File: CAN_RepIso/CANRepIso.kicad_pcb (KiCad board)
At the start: 4 copper layers, 60 x 27 mm, 53 parts, among them J1 RBUS_IN, J2 RBUS_OUT, U1 SN74LV32ADGVR, U2 SN74LVC2G08DCUR, U3 SN74LVC2G07DBVR, U4 SN74LVC2G07DBVR, U5 SN74LVC2G132DCUR, U6 SN65HVD230, U7 PLACEHOLDER ISOLATOR, U8 SN65HVD230

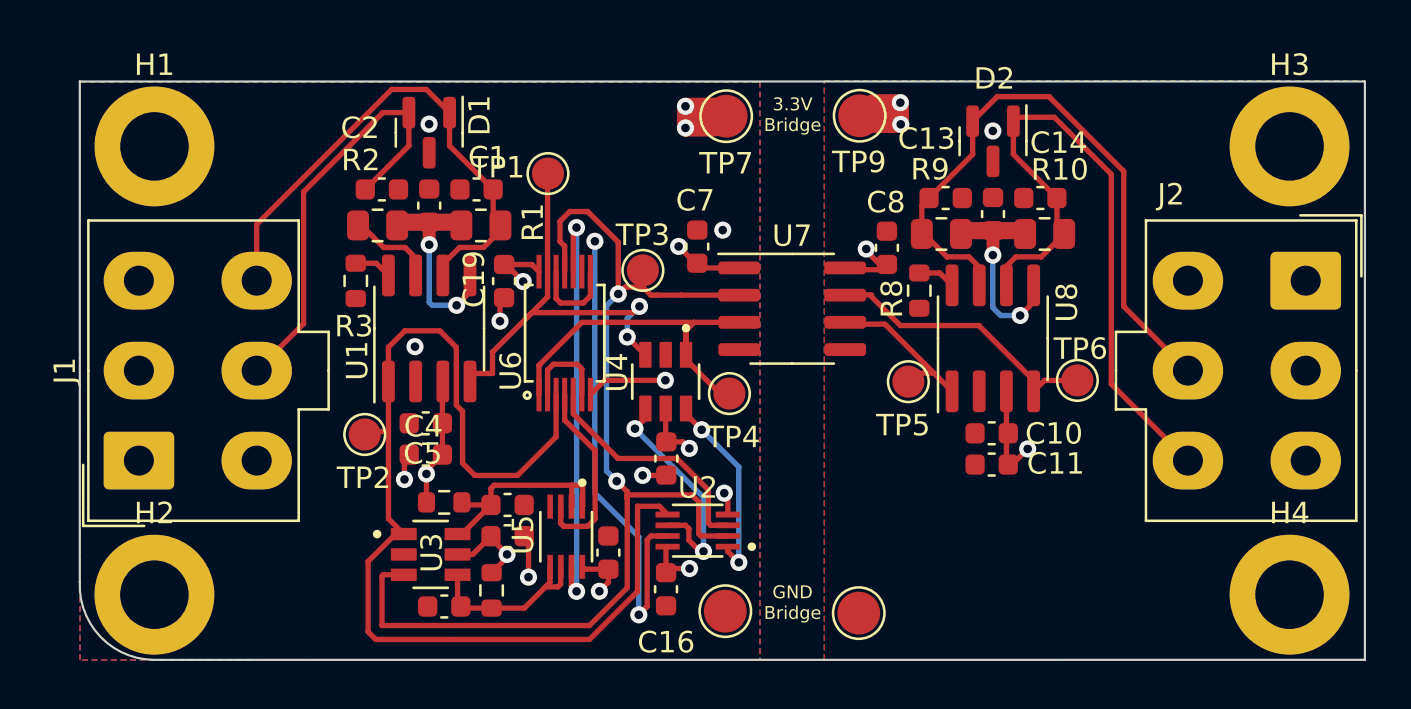
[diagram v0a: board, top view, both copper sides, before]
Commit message: Rounded corners + via stitching
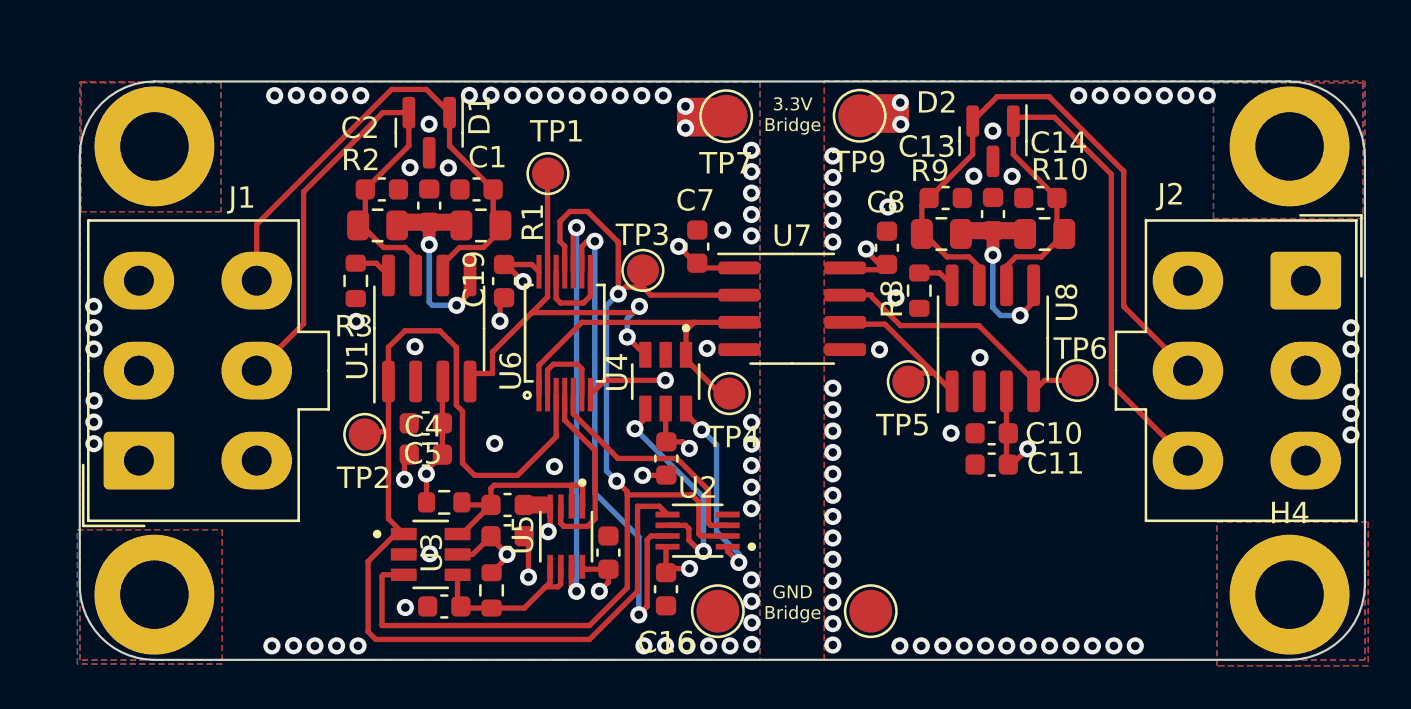
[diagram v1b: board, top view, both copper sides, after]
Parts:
- moved TP10 0.57 mm to (69.7, 106.5)
- moved TP8 0.35 mm to (62.5, 106.5)
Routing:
- net +3V3: track 31.8 -> 28.7 mm
- net /CAN_LOW_IN: track 26.2 -> 23.8 mm
- net +3.3VA: track 15.2 -> 12.8 mm
- net Net-(U1-Pad9): track 23.0 -> 24.9 mm
- net /Vref: track 9.87 -> 8.61 mm
- net /Vref2: track 9.73 -> 8.51 mm
- net /CAN_HIGH_OUT: track 29.9 -> 29.0 mm
- net /TX2: track 16.9 -> 16.1 mm
- net /CAN_LOW_OUT: track 31.3 -> 30.6 mm
- net /TX1: track 51.5 -> 50.9 mm
- net Net-(TP5-Pad1): track 7.65 -> 7.08 mm
- net Net-(TP6-Pad1): track 13.2 -> 12.7 mm
- net GND: track 10.4 -> 10.7 mm, vias 9 -> 62
- net GND1: vias 1 -> 50
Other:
- outline, holes or cut-outs redrawn

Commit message: changed U4 from driver to NOT gate, implemented review feedback
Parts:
- U4: value SN74LVC2G07DBVR -> SN74LVC2G04DBVR
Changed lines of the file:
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@@
     (property "Sheetname" "Bus Arbitration")
     (attr smd)
-    (fp_text reference "R12" (at 0.3 -1.3925 90) (layer "F.SilkS") hide
+    (fp_text reference "R12" (at 0.12 -1.3825 90) (layer "F.SilkS")
       (effects (font (size 1 1) (thickness 0.15)))
     )
@@
     (property "Sheetname" "Bus Arbitration")
     (attr through_hole)
-    (fp_text reference "U4" (at -0.43 2.26 -90) (layer "F.SilkS")
-      (effects (font (size 1 1) (thickness 0.15)))
-    )
-    (fp_text value "SN74LVC2G07DBVR" (at 7.26 2.365 90) (layer "F.Fab")
+    (fp_text reference "U4" (at 0.375 -2.635 -90) (layer "F.SilkS")
+      (effects (font (size 1 1) (thickness 0.15)))
+    )
+    (fp_text value "SN74LVC2G04DBVR" (at 7.26 2.365 -90) (layer "F.Fab")
       (effects (font (size 1 1) (thickness 0.15)))
     )
@@
     (fp_line (start -0.8 1.56) (end 0.8 1.56) (layer "F.SilkS") (width 0.127))
     (fp_circle (center -2.5 -0.95) (end -2.4 -0.95) (layer "F.SilkS") (width 0.2) (fill none))
-    (fp_line (start 2.11 1.49) (end 1.05 1.49) (layer "F.CrtYd") (width 0.05))
-    (fp_line (start 1.05 -1.49) (end 1.05 -1.7) (layer "F.CrtYd") (width 0.05))
-    (fp_line (start -1.05 1.7) (end 1.05 1.7) (layer "F.CrtYd") (width 0.05))
     (fp_line (start 1.05 1.49) (end 1.05 1.7) (layer "F.CrtYd") (width 0.05))
     (fp_line (start -2.11 -1.49) (end -2.11 1.49) (layer "F.CrtYd") (width 0.05))
+    (fp_line (start -1.05 -1.49) (end -1.05 -1.7) (layer "F.CrtYd") (width 0.05))
+    (fp_line (start 2.11 -1.49) (end 1.05 -1.49) (layer "F.CrtYd") (width 0.05))
     (fp_line (start 1.05 -1.7) (end -1.05 -1.7) (layer "F.CrtYd") (width 0.05))
+    (fp_line (start -1.05 1.49) (end -1.05 1.7) (layer "F.CrtYd") (width 0.05))
     (fp_line (start -2.11 -1.49) (end -1.05 -1.49) (layer "F.CrtYd") (width 0.05))
-    (fp_line (start -1.05 1.49) (end -1.05 1.7) (layer "F.CrtYd") (width 0.05))
     (fp_line (start -2.11 1.49) (end -1.05 1.49) (layer "F.CrtYd") (width 0.05))
-    (fp_line (start 2.11 -1.49) (end 1.05 -1.49) (layer "F.CrtYd") (width 0.05))
-    (fp_line (start -1.05 -1.49) (end -1.05 -1.7) (layer "F.CrtYd") (width 0.05))
+    (fp_line (start -1.05 1.7) (end 1.05 1.7) (layer "F.CrtYd") (width 0.05))
+    (fp_line (start 1.05 -1.49) (end 1.05 -1.7) (layer "F.CrtYd") (width 0.05))
+    (fp_line (start 2.11 1.49) (end 1.05 1.49) (layer "F.CrtYd") (width 0.05))
     (fp_line (start 2.11 1.49) (end 2.11 -1.49) (layer "F.CrtYd") (width 0.05))
     (fp_line (start 0.8 -1.45) (end -0.8 -1.45) (layer "F.Fab") (width 0.127))
+    (fp_line (start -0.8 -1.45) (end -0.8 1.45) (layer "F.Fab") (width 0.127))
     (fp_line (start -0.8 1.45) (end 0.8 1.45) (layer "F.Fab") (width 0.127))
-    (fp_line (start -0.8 -1.45) (end -0.8 1.45) (layer "F.Fab") (width 0.127))
     (fp_line (start 0.8 1.45) (end 0.8 -1.45) (layer "F.Fab") (width 0.127))
     (fp_circle (center -2.5 -0.95) (end -2.4 -0.95) (layer "F.Fab") (width 0.2) (fill none))
@@
     (property "Sheetname" "Bus Arbitration")
     (attr smd)
-    (fp_text reference "R11" (at 0.08 0.01) (layer "F.SilkS") hide
+    (fp_text reference "R11" (at -2.8425 0.07) (layer "F.SilkS")
       (effects (font (size 1 1) (thickness 0.15)))
     )
@@
     (property "Sheetname" "Bus Arbitration")
     (attr smd)
-    (fp_text reference "C21" (at -0.1025 -0.01) (layer "F.SilkS") hide
+    (fp_text reference "C21" (at 0.0075 -1.36) (layer "F.SilkS")
       (effects (font (size 1 1) (thickness 0.15)))
     )
@@
     (property "Sheetname" "Bus Arbitration")
     (attr smd)
-    (fp_text reference "C18" (at 3 0.01) (layer "F.SilkS") hide
+    (fp_text reference "C18" (at 0.8375 -1.420292) (layer "F.SilkS")
       (effects (font (size 1 1) (thickness 0.15)))
     )
@@
     (property "Sheetname" "")
     (attr exclude_from_pos_files)
-    (fp_text reference "H4" (at 0 -3.8) (layer "F.SilkS")
+    (fp_text reference "H4" (at 0 -3.8) (layer "F.SilkS") hide
       (effects (font (size 1 1) (thickness 0.15)))
     )
@@
     (property "Sheetname" "")
     (attr smd)
-    (fp_text reference "C5" (at 0.14 0.04) (layer "F.SilkS")
+    (fp_text reference "C5" (at -2.435 -0.36) (layer "F.SilkS")
       (effects (font (size 1 1) (thickness 0.15)))
     )
@@
     (property "Sheetname" "Bus Arbitration")
     (attr through_hole)
-    (fp_text reference "U3" (at 0.0575 -0.08 270) (layer "F.SilkS")
+    (fp_text reference "U3" (at -2.8125 0.63 270) (layer "F.SilkS")
       (effects (font (size 1 1) (thickness 0.15)))
     )
@@
     (property "Sheetname" "")
     (attr smd)
-    (fp_text reference "C4" (at 0.11 -0.15) (layer "F.SilkS")
+    (fp_text reference "C4" (at -2.435 0.03) (layer "F.SilkS")
       (effects (font (size 1 1) (thickness 0.15)))
     )
@@
     (property "Sheetname" "Bus Arbitration")
     (attr through_hole)
-    (fp_text reference "U1" (at -1.28 -9.68 90) (layer "F.SilkS")
+    (fp_text reference "U1" (at -1.88 -2.61 90) (layer "F.SilkS")
       (effects (font (size 1.001543 1.001543) (thickness 0.15)))
     )
@@
     (property "Sheetname" "Bus Arbitration")
     (attr smd)
-    (fp_text reference "C19" (at -0.09 1.4 90) (layer "F.SilkS")
+    (fp_text reference "C19" (at 2.1 -0.69 180) (layer "F.SilkS")
       (effects (font (size 1 1) (thickness 0.15)))
     )
@@
     (property "Sheetname" "")
     (attr smd)
-    (fp_text reference "U6" (at -1.99 3.815 90) (layer "F.SilkS")
+    (fp_text reference "U6" (at -2.04 -3.285 90) (layer "F.SilkS")
       (effects (font (size 1 1) (thickness 0.15)))
     )
@@
     (property "Sheetname" "Bus Arbitration")
     (attr through_hole)
-    (fp_text reference "U5" (at -0.09 2.01 90) (layer "F.SilkS")
+    (fp_text reference "U5" (at 3.405 0.2 180) (layer "F.SilkS")
       (effects (font (size 1 1) (thickness 0.15)))
     )
@@
     )
   )
-  (gr_arc (start 32.739117 85.205342) (mid 33.76 82.74) (end 36.225003 81.718297) (layer "Edge.Cuts") (width 0.1))
+  (gr_arc (start 32.739117 85.205342) (mid 33.76 82.739999) (end 36.225003 81.718297) (layer "Edge.Cuts") (width 0.1))
   (gr_line (start 32.739117 85.205342) (end 32.739521 105.084438) (layer "Edge.Cuts") (width 0.1))
   (gr_arc (start 89.219839 81.72) (mid 91.70913 82.752606) (end 92.74 85.242616) (layer "Edge.Cuts") (width 0.1))

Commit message: Added text and logos
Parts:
- added G***: LOGO, iclr:iclr_logo, F.Cu at (78.3, 104.1)
- added G***: LOGO, iclr:spider-man, B.Cu at (65.1, 95.9)
- renumbered J1 to RBUS1, J2 to RBUS2
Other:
- board text added: "CAN BUS REPEATER"
- board text added: "Designed By Andrei Paduraru Electronics and Payload 2022"
- board text added: "Isolator?"
- board text added: "JLCJLCJLCJLC"
- board text added: "No"
- board text added: "Yes"

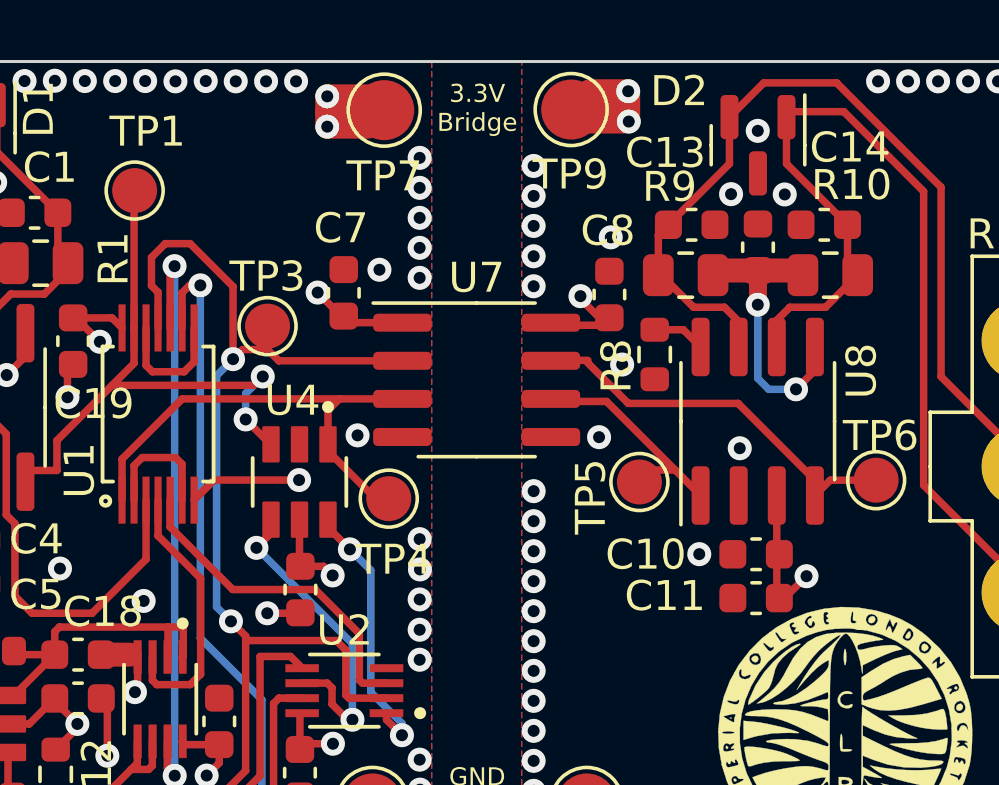
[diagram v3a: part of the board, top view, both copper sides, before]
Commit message: added option for a 2nd digital isolator
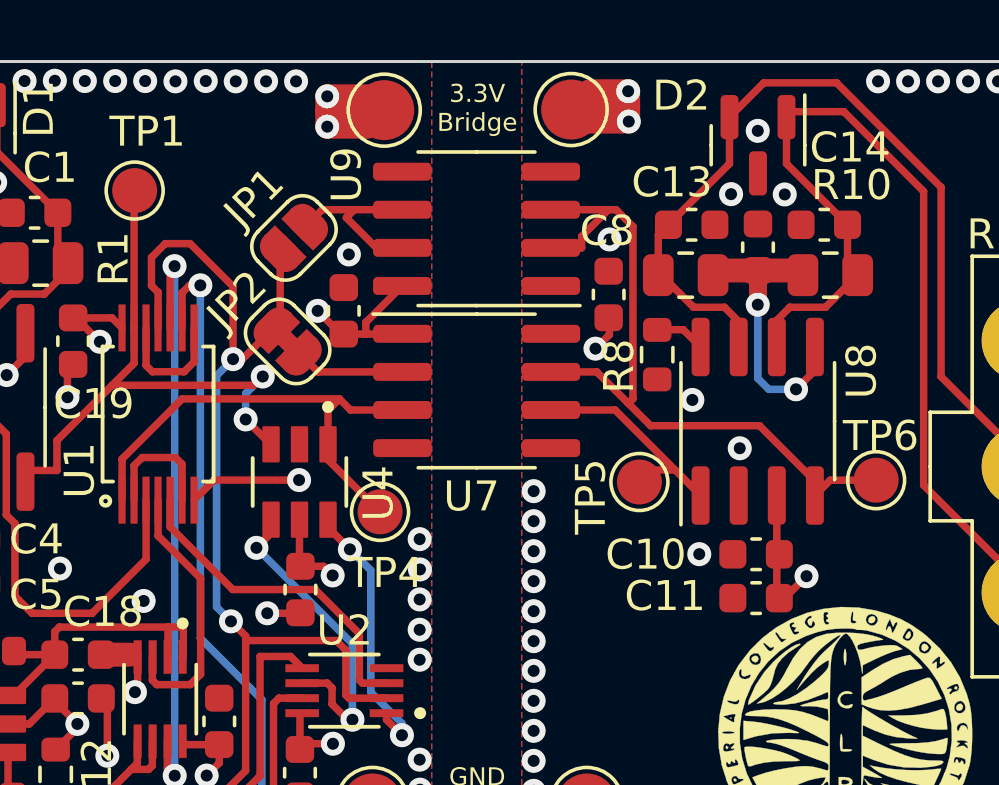
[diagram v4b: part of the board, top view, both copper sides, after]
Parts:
- removed TP3: TestPoint, TestPoint:TestPoint_Pad_D1.5mm
- added JP1: SolderJumper_2_Open, Jumper:SolderJumper-2_P1.3mm_Open_RoundedPad1.0x1.5mm, F.Cu at (59.9, 87.6)
- added JP2: SolderJumper_2_Bridged, Jumper:SolderJumper-2_P1.3mm_Bridged_RoundedPad1.0x1.5mm, F.Cu at (59.7, 91.1)
- added U9: ADuM120N, Package_SO:SOIC-8_3.9x4.9mm_P1.27mm, F.Cu at (66.0, 87.3)
- moved C7 0.60 mm to (61.6, 90.0)
- moved TP4 0.53 mm to (62.8, 96.7)
- moved U7 0.37 mm to (66.0, 92.7)
- moved R8 0.09 mm to (72.0, 91.5)
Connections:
- U7 pad 2: /RX2 -> Net-(TP3-Pad1)
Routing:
- net Net-(TP6-Pad1): track 12.7 -> 24.6 mm
- net Net-(U9-Pad6): track 0.00 -> 6.00 mm
- net Net-(TP3-Pad1): track 0.00 -> 3.59 mm
- net +3V3: track 28.7 -> 31.1 mm
- net /RX2: track 51.3 -> 49.0 mm
- net +3.3VA: track 12.8 -> 11.4 mm
- net GND1: vias 50 -> 44
- net GND: vias 62 -> 56

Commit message: v2 finished pre-review
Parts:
- removed the G*** at (78.3, 104.1)
- added C22: 2.2uF, Capacitor_SMD:C_0402_1005Metric, F.Cu at (156.3, 87.0)
- added C23: 2.2uF, Capacitor_SMD:C_0402_1005Metric, F.Cu at (124.7, 86.8)
- added C6: 1pF, Capacitor_SMD:C_0402_1005Metric, F.Cu at (152.5, 93.1)
- added C9: 1pF, Capacitor_SMD:C_0402_1005Metric, F.Cu at (154.4, 97.2)
- added D3: RX1LED, LED_SMD:LED_0402_1005Metric, F.Cu at (132.5, 101.1)
- added D4: TX1LED, LED_SMD:LED_0402_1005Metric, F.Cu at (126.1, 101.1)
- added D5: RX2LED, LED_SMD:LED_0402_1005Metric, F.Cu at (152.5, 92.2)
- added D6: TX2LED, LED_SMD:LED_0402_1005Metric, F.Cu at (149.4, 101.8)
- added D7: 3V31LED, LED_SMD:LED_0402_1005Metric, F.Cu at (121.4, 85.0)
- added D8: 3V32LED, LED_SMD:LED_0402_1005Metric, F.Cu at (155.5, 85.7)
- added G***: LOGO, LOGO, B.Cu at (122.0, 105.8)
- added JP3: SolderJumper_2_Bridged, Jumper:SolderJumper-2_P1.3mm_Bridged_RoundedPad1.0x1.5mm, B.Cu at (160.5, 89.6)
- added JP4: SolderJumper_2_Bridged, Jumper:SolderJumper-2_P1.3mm_Bridged_RoundedPad1.0x1.5mm, B.Cu at (121.1, 89.5)
- added R13: 470, Resistor_SMD:R_0402_1005Metric, F.Cu at (123.3, 85.0)
- added R14: 470, Resistor_SMD:R_0402_1005Metric, F.Cu at (155.0, 87.1)
- added R15: 0, Resistor_SMD:R_0402_1005Metric, F.Cu at (133.2, 91.5)
- added R16: 0, Resistor_SMD:R_0402_1005Metric, F.Cu at (151.1, 105.5)
- added R4: 1k, Resistor_SMD:R_0402_1005Metric, F.Cu at (131.4, 102.0)
- added R5: 1k, Resistor_SMD:R_0402_1005Metric, F.Cu at (126.1, 102.0)
- added R6: 1k, Resistor_SMD:R_0402_1005Metric, F.Cu at (152.5, 91.2)
- added R7: 1k, Resistor_SMD:R_0402_1005Metric, F.Cu at (149.4, 103.6)
- added TP11: TestPoint, Connector_PinHeader_2.54mm:PinHeader_1x01_P2.54mm_Vertical, F.Cu at (143.2, 88.2)
- added TP12: TestPoint, Connector_PinHeader_2.54mm:PinHeader_1x01_P2.54mm_Vertical, F.Cu at (149.0, 88.2)
- added TP3: TestPoint, TestPoint:TestPoint_Pad_D1.0mm, F.Cu at (140.5, 97.0)
- added U10: AP2205-33W5-7, iclr:SOT95P282X145-5N, F.Cu at (122.1, 87.2)
- added U11: AP2205-33W5-7, iclr:SOT95P282X145-5N, F.Cu at (158.9, 86.5)
- C1: value 220 pF -> 1pF; footprint Capacitor_SMD:C_0603_1608Metric -> Capacitor_SMD:C_0402_1005Metric
- C10, C11, C15, C16, C17, C18, C19, C20, C21, C4, C5, C7, C8: footprint Capacitor_SMD:C_0603_1608Metric -> Capacitor_SMD:C_0402_1005Metric
- C12, C3: value 0.1uF -> 47nF; footprint Capacitor_SMD:C_0603_1608Metric -> Capacitor_SMD:C_0402_1005Metric
- C13: value 220pF -> 1uF; footprint Capacitor_SMD:C_0603_1608Metric -> Capacitor_SMD:C_0402_1005Metric
- C14: value 220 pF -> 1uF; footprint Capacitor_SMD:C_0603_1608Metric -> Capacitor_SMD:C_0402_1005Metric
- C2: value 220pF -> 1pF; footprint Capacitor_SMD:C_0603_1608Metric -> Capacitor_SMD:C_0402_1005Metric
- R1, R10, R2, R9: footprint Resistor_SMD:R_0805_2012Metric -> Resistor_SMD:R_0603_1608Metric
- R11, R12: footprint Resistor_SMD:R_0603_1608Metric -> Resistor_SMD:R_0402_1005Metric
- R3, R8: value 10k -> 0
- RBUS1, RBUS2: footprint Connector_Molex:Molex_Mini-Fit_Jr_5566-06A_2x03_P4.20mm_Vertical -> Connector_Molex:Molex_Mini-Fit_Jr_5569-06A2_2x03_P4.20mm_Horizontal
- TP1, TP2, TP4, TP5, TP6: footprint TestPoint:TestPoint_Pad_D1.5mm -> TestPoint:TestPoint_Pad_D1.0mm
- TP10, TP7, TP8, TP9: footprint TestPoint:TestPoint_Pad_D2.0mm -> Connector_PinHeader_2.54mm:PinHeader_1x01_P2.54mm_Vertical
- moved R8 88.3 mm to (159.3, 104.6), turned to 0 degrees
- moved D2 86.7 mm to (159.1, 107.1), turned to 180 degrees
- moved R9 84.4 mm to (155.7, 105.8)
- moved C14 83.8 mm to (161.4, 87.0), turned to 90 degrees
- moved TP5 83.4 mm to (154.8, 95.8)
- moved C1 83.3 mm to (133.5, 100.2)
- moved C17 83.3 mm to (134.0, 84.5), turned to 180 degrees
- moved C12 83.1 mm to (156.2, 107.0), turned to 0 degrees
- moved RBUS1 81.8 mm to (117.3, 100.7)
- moved G*** 81.6 mm to (146.7, 97.4)
- moved R2 81.4 mm to (128.1, 89.8)
- moved C4 81.3 mm to (130.2, 99.1)
- moved C5 81.3 mm to (130.2, 100.0)
- moved R3 81.1 mm to (126.6, 95.6)
- moved U6 81.0 mm to (130.0, 94.9)
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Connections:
- net Net-(TP5-Pad1) renamed /TX2_PRE_ISO
- net Net-(TP6-Pad1) renamed /RX2_PRE_ISO
- C1 pad 1: GND -> /RX1
- C1 pad 2: /CAN_LOW_IN -> GND
- C13 pad 1: GND1 -> /RBUS_uC_V1
- C13 pad 2: /CAN_HIGH_OUT -> GND
- C14 pad 1: GND1 -> /RBUS_uC_V2
- C14 pad 2: /CAN_LOW_OUT -> GND1
- C2 pad 1: GND -> /TX1
- C2 pad 2: /CAN_HIGH_IN -> GND
- D1 pad 1: /CAN_LOW_IN -> /CAN_IN_-
- D1 pad 2: /CAN_HIGH_IN -> /CAN_IN_+
- D2 pad 1: /CAN_LOW_OUT -> /CAN_OUT_-
- D2 pad 2: /CAN_HIGH_OUT -> /CAN_OUT_+
- JP1 pad 1: /RX2 -> /TX2
- JP2 pad 1: /RX2 -> /TX2
- R1 pad 2: /CAN_LOW_IN -> /CAN_IN_-
- R10 pad 2: /CAN_LOW_OUT -> /CAN_OUT_-
- R2 pad 1: /CAN_HIGH_IN -> /CAN_IN_+
- R9 pad 1: /CAN_HIGH_OUT -> /CAN_OUT_+
- RBUS1 pad 3: +3V3 -> /RBUS_uC_V1
- RBUS1 pad 4: unconnected-(RBUS1-Pad4) -> /Deploy1
- RBUS1 pad 5: /CAN_HIGH_IN -> /CAN_IN_+
- RBUS1 pad 6: /CAN_LOW_IN -> /CAN_IN_-
- RBUS2 pad 3: +3.3VA -> /RBUS_uC_V2
- RBUS2 pad 4: unconnected-(RBUS2-Pad4) -> /Deploy2
- RBUS2 pad 5: /CAN_HIGH_OUT -> /CAN_OUT_+
- RBUS2 pad 6: /CAN_LOW_OUT -> /CAN_OUT_-
- TP4 pad 1: /TX2 -> /RX2
- U6 pad 5: /Vref -> Net-(U6-Vref)
- U6 pad 6: /CAN_LOW_IN -> /CAN_IN_-
- U6 pad 7: /CAN_HIGH_IN -> /CAN_IN_+
- U7 pad 3: /TX2 -> /RX2
- U8 pad 5: /Vref2 -> Net-(U8-Vref)
- U8 pad 6: /CAN_LOW_OUT -> /CAN_OUT_-
- U8 pad 7: /CAN_HIGH_OUT -> /CAN_OUT_+
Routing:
- net /RBUS_uC_V2: track 0.00 -> 34.8 mm
- net /CAN_LOW_OUT: track 30.6 -> 0.00 mm
- net /CAN_OUT_-: track 0.00 -> 29.8 mm
- net /CAN_HIGH_OUT: track 29.0 -> 0.00 mm
- net /CAN_OUT_+: track 0.00 -> 28.3 mm
- net /CAN_IN_-: track 0.00 -> 27.2 mm
- net /CAN_IN_+: track 0.00 -> 26.6 mm
- net /Deploy1: track 0.00 -> 26.3 mm
- net /CAN_HIGH_IN: track 24.6 -> 0.00 mm
- net /CAN_LOW_IN: track 23.8 -> 0.00 mm
- net Net-(U1-3B): track 20.4 -> 40.3 mm, vias 2 -> 0
- net /RBUS_uC_V1: track 0.00 -> 16.7 mm
- net /TX1: track 50.9 -> 35.7 mm, vias 0 -> 2
- net Net-(U1-2A): track 8.98 -> 20.4 mm, vias 0 -> 2
- net /Deploy2: track 0.00 -> 10.7 mm
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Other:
- board size 60 x 27 mm -> 57 x 27 mm
- board text added: "DEPLOY Bridge"
- board text added: "Designed By Andrei Paduraru Electronics and Payload 2023"
- board text added: "REPEATER 2.0"
- board text added: "THE COULDN'T"
- board text removed: "CAN BUS REPEATER"
- board text removed: "Designed By Andrei Paduraru Electronics and Payload 2022"
- board text removed: "Isolator?"
- board text removed: "No"
- board text removed: "Yes"
